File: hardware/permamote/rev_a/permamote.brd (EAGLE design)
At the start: 27 x 60.1 mm, 131 parts, among them J1 TC2030-JLINK-NL, J5 MICRO_USB_B_HIROSE_ZX62R-B-5P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, Q1 PMDXB950UPEL, Q10 PMDXB950UPEL, Q2 PMDXB950UPEL, Q3 PMDXB950UPEL, Q4 PMDXB950UPEL, Q5 PMDXB950UPEL, Q6 PMDXB950UPEL, Q7 PMDXB950UPEL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

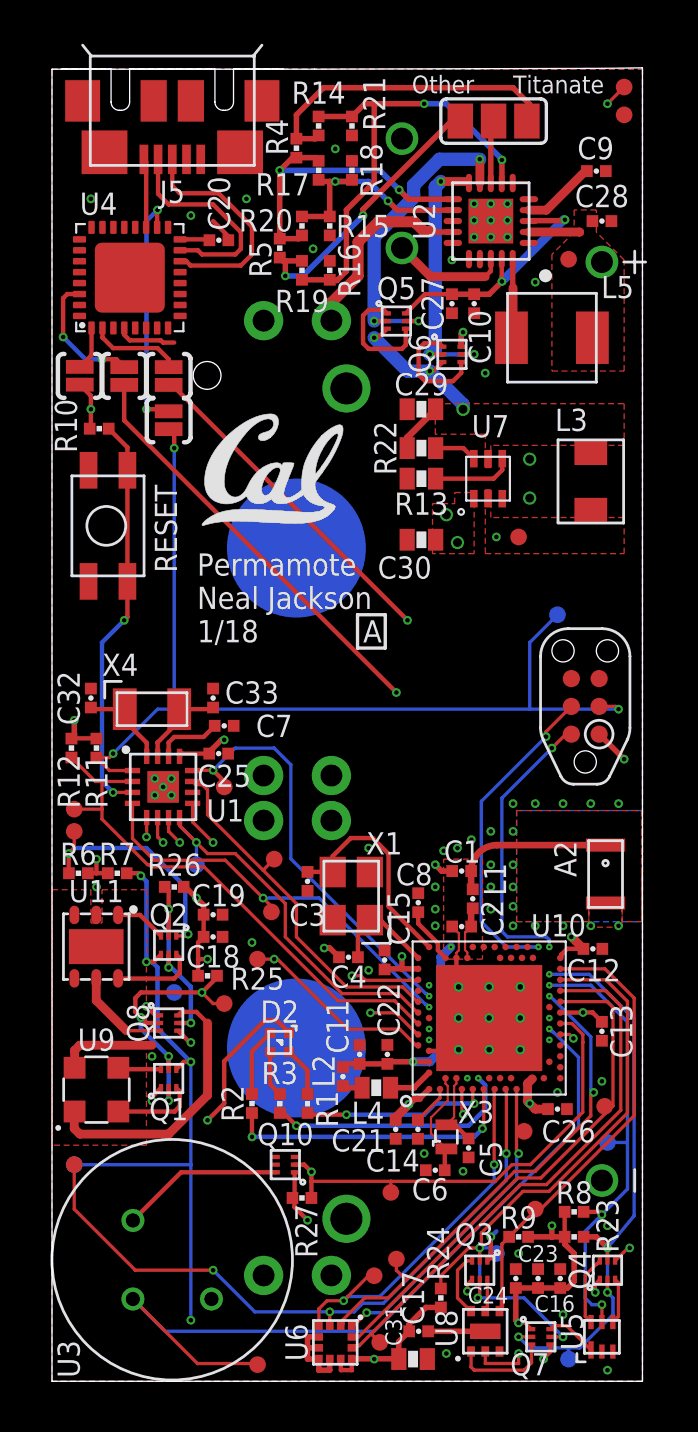
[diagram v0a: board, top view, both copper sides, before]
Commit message: Change attributes to include MPN, fix up BOM
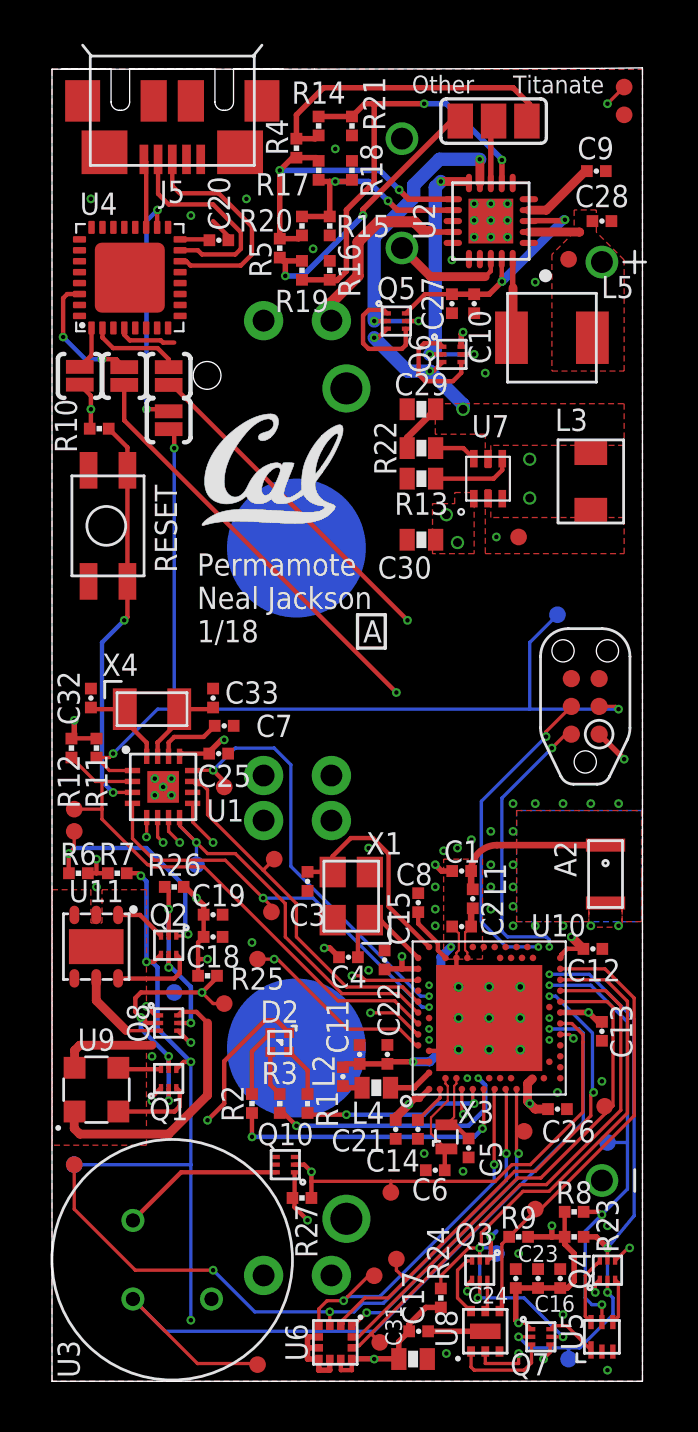
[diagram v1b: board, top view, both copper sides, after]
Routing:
- net PIR_OUT: track 36.9 -> 37.8 mm

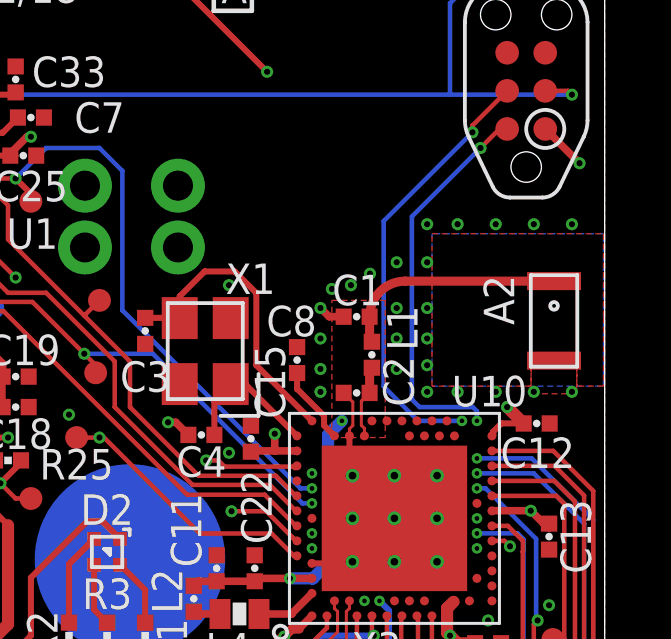
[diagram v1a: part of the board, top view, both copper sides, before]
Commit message: Fix NRF52840 via drill size
Update BOM
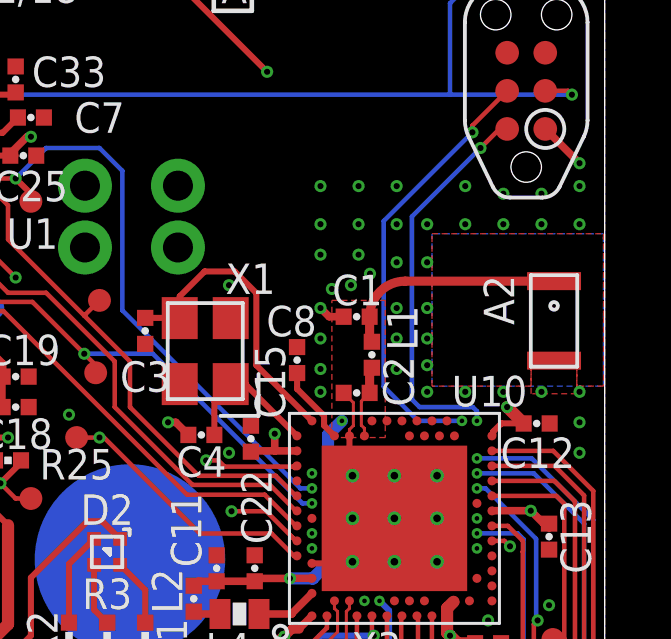
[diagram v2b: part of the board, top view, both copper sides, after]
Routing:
- net GND: track 31.5 -> 31.6 mm, vias 74 -> 88

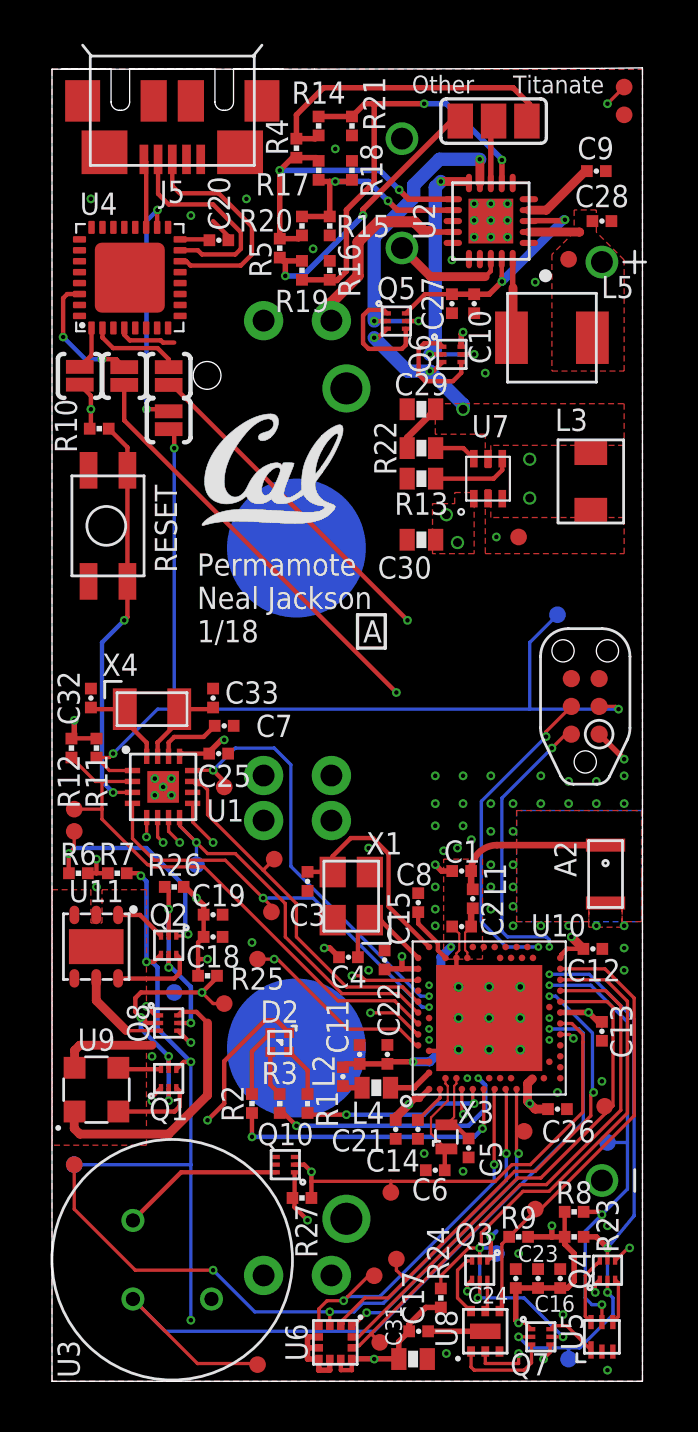
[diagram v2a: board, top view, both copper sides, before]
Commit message: Move silk+testpoints
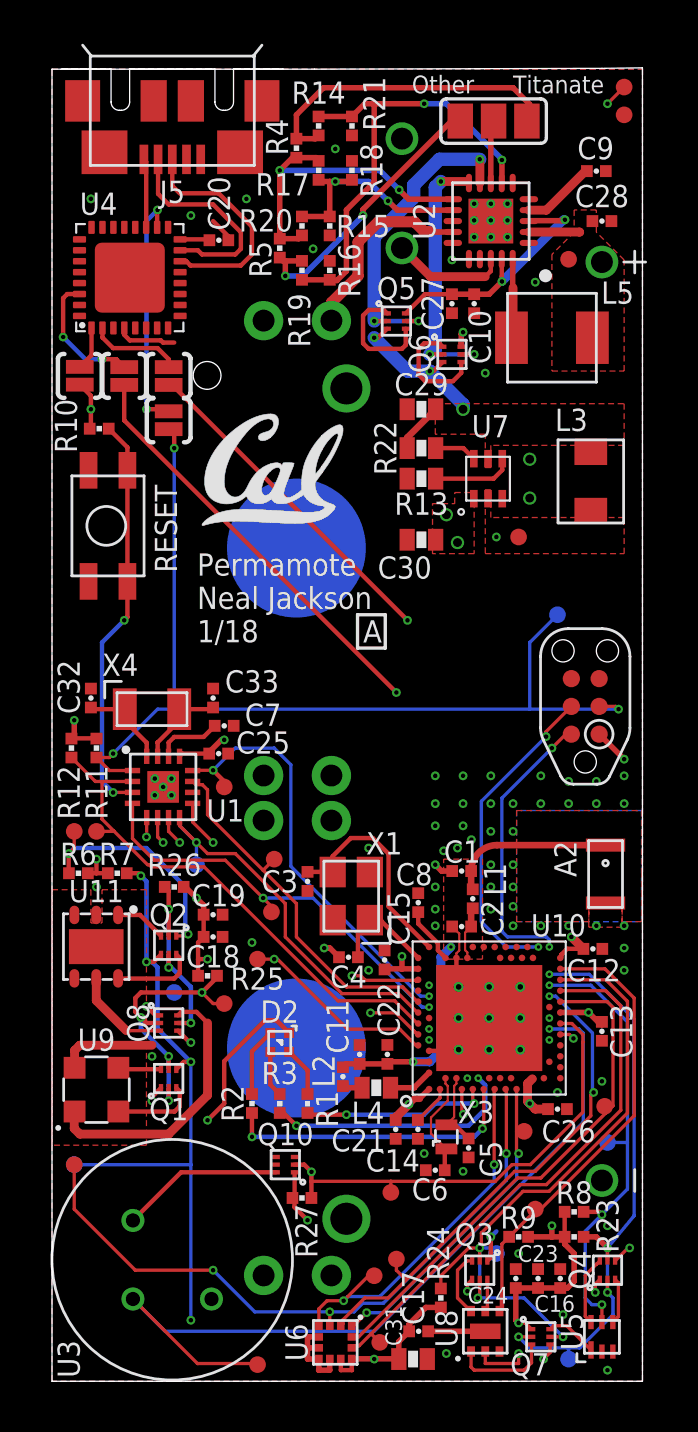
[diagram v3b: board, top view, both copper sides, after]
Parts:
- moved TP16 1.44 mm to (2.03, 25.1)
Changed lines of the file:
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@@
 <?xml version="1.0" encoding="utf-8"?>
 <!DOCTYPE eagle SYSTEM "eagle.dtd">
-<eagle version="8.5.2">
+<eagle version="8.6.0">
 <drawing>
 <settings>
@@
 <attribute name="DIGIKEY" value="490-6197-1-ND" x="11.684" y="22.86" size="1.778" layer="27" rot="R90" display="off"/>
 <attribute name="MPN" value="GRM1555C1H120GA01D " x="11.684" y="22.86" size="1.778" layer="27" rot="R90" display="off"/>
-<attribute name="NAME" x="11.684" y="21.844" size="1.016" layer="25" font="vector" ratio="12" rot="R180" align="bottom-center"/>
+<attribute name="NAME" x="10.414" y="22.352" size="1.016" layer="25" font="vector" ratio="12" align="bottom-center"/>
 </element>
 <element name="C4" library="passives" package="0402_CAP" value="12pF" x="13.557" y="19.392" smashed="yes">
@@
 </element>
 <element name="BT1" library="batteries" package="1020" value="LTOHTC1020" x="16.002" y="54.324" smashed="yes" rot="MR90">
-<attribute name="NAME" x="11.43" y="49.156" size="1.016" layer="22" font="vector" ratio="12" rot="MR0" align="bottom-center"/>
+<attribute name="NAME" x="11.43" y="49.156" size="1.016" layer="26" font="vector" ratio="12" rot="MR0" align="bottom-center"/>
 </element>
 <element name="BT4" library="batteries" package="BH123A" value="BAT_PACKCR123A" x="13.462" y="26.416" smashed="yes" rot="MR90">
@@
 <attribute name="MANUFACTURER" value="MPD" x="13.462" y="26.416" size="1.778" layer="28" rot="MR90" display="off"/>
 <attribute name="MPN" value="BH123A" x="13.462" y="26.416" size="1.778" layer="28" rot="MR90" display="off"/>
-<attribute name="NAME" x="22.606" y="4.826" size="1.016" layer="22" font="vector" ratio="12" rot="MR90"/>
+<attribute name="NAME" x="22.606" y="4.826" size="1.016" layer="26" font="vector" ratio="12" rot="MR90"/>
 </element>
 <element name="U5" library="chips" package="ODFN-6-1.5MMX1.6MM" value="ISL29125" x="25.146" y="2.032" smashed="yes" rot="R90">
@@
 <attribute name="DIGIKEY" value="490-5942-1-ND" x="4.064" y="36.322" size="1.778" layer="27" display="off"/>
 <attribute name="MPN" value="GRM1555C1H470JA01D " x="7.874" y="29.972" size="1.778" layer="27" display="off"/>
-<attribute name="NAME" x="10.16" y="29.464" size="1.016" layer="25" font="vector" ratio="12" align="bottom-center"/>
+<attribute name="NAME" x="9.652" y="29.972" size="1.016" layer="25" font="vector" ratio="12" align="bottom-center"/>
 </element>
 <element name="X4" library="crystals" package="2-SMD" value="ABS07-32.768KHZ-7-T" x="4.572" y="30.734" smashed="yes">
@@
 </element>
 <element name="C32" library="passives" package="0402_CAP" value="DNP" x="1.778" y="31.242" smashed="yes" rot="R90">
-<attribute name="NAME" x="1.27" y="31.242" size="1.016" layer="25" font="vector" ratio="12" rot="R90" align="bottom-center"/>
+<attribute name="NAME" x="1.27" y="31.75" size="1.016" layer="25" font="vector" ratio="12" rot="R90" align="bottom-center"/>
 </element>
 <element name="C33" library="passives" package="0402_CAP" value="DNP" x="7.366" y="31.242" smashed="yes" rot="R90">
-<attribute name="NAME" x="9.144" y="30.988" size="1.016" layer="25" font="vector" ratio="12" align="bottom-center"/>
+<attribute name="NAME" x="9.144" y="31.496" size="1.016" layer="25" font="vector" ratio="12" align="bottom-center"/>
 </element>
 <element name="C25" library="passives" package="0402_CAP" value="1uF" x="7.62" y="28.702" smashed="yes">
 <attribute name="DIGIKEY" value="490-7195-1-ND " x="-2.54" y="27.432" size="1.778" layer="27" display="off"/>
 <attribute name="MPN" value="GRM155R70G105KA12D " x="7.62" y="28.702" size="1.778" layer="27" display="off"/>
-<attribute name="NAME" x="7.874" y="28.194" size="1.016" layer="25" font="vector" ratio="12" rot="R180" align="bottom-center"/>
+<attribute name="NAME" x="9.652" y="29.718" size="1.016" layer="25" font="vector" ratio="12" rot="R180" align="bottom-center"/>
 </element>
 <element name="C17" library="passives" package="0402_CAP" value="0.1uF" x="16.764" y="2.286" smashed="yes">
@@
 <attribute name="DIGIKEY" value="732-3340-1-ND" x="22.86" y="47.72" size="1.778" layer="27" rot="R180" display="off"/>
 <attribute name="MPN" value="74437324220 " x="22.86" y="47.72" size="1.778" layer="27" rot="R180" display="off"/>
-<attribute name="NAME" x="25.114" y="49.53" size="1.016" layer="25" font="vector" ratio="12"/>
+<attribute name="NAME" x="25.114" y="49.276" size="1.016" layer="25" font="vector" ratio="12"/>
 <attribute name="VALUE" x="26.035" y="52.8" size="1.27" layer="27" rot="R180"/>
 </element>
@@
 <attribute name="DIGIKEY" value="311-10KJRCT-ND " x="2.032" y="28.956" size="1.778" layer="27" rot="R90" display="off"/>
 <attribute name="MPN" value="RC0402JR-0710KL" x="2.032" y="28.956" size="1.778" layer="27" rot="R90" display="off"/>
-<attribute name="NAME" x="2.54" y="27.432" size="1.016" layer="25" font="vector" ratio="12" rot="R90" align="bottom-center"/>
+<attribute name="NAME" x="2.54" y="26.924" size="1.016" layer="25" font="vector" ratio="12" rot="R90" align="bottom-center"/>
 <attribute name="VALUE" x="3.429" y="28.956" size="1.016" layer="27" font="vector" ratio="12" rot="R90" align="bottom-center"/>
 </element>
@@
 <attribute name="MOUSER" value="712-BAT-HLD-001-THM" x="11.176" y="15.24" size="1.778" layer="28" rot="MR270" display="off"/>
 <attribute name="MPN" value="BAT-HLD-001-THM" x="11.176" y="15.24" size="1.778" layer="28" rot="MR270" display="off"/>
-<attribute name="NAME" x="21.844" y="15.24" size="1.016" layer="26" font="vector" ratio="12" rot="MR90" align="bottom-center"/>
+<attribute name="NAME" x="17.018" y="24.384" size="1.016" layer="26" font="vector" ratio="12" rot="MR0" align="bottom-center"/>
 </element>
 <element name="BT3" library="batteries" package="BAT-HLD-002-THM" value="BAT-HLD-002-THM" x="11.176" y="38.1" smashed="yes" rot="MR270">
@@
 <attribute name="MOUSER" value="712-BAT-HLD-001-THM" x="11.176" y="38.1" size="1.778" layer="28" rot="MR270" display="off"/>
 <attribute name="MPN" value="BAT-HLD-001-THM" x="11.176" y="38.1" size="1.778" layer="28" rot="MR270" display="off"/>
-<attribute name="NAME" x="21.803" y="38.1" size="1.016" layer="26" font="vector" ratio="12" rot="MR90" align="bottom-center"/>
+<attribute name="NAME" x="17.018" y="27.94" size="1.016" layer="26" font="vector" ratio="12" rot="MR0" align="bottom-center"/>
 </element>
 <element name="R19" library="passives" package="0402_RES" value="DNP" x="11.43" y="50.8" smashed="yes" rot="R90">
 <attribute name="DIGIKEY" value="YAG3306CT-ND" x="11.43" y="50.8" size="1.778" layer="27" font="vector" ratio="12" rot="R90" display="off"/>
-<attribute name="NAME" x="11.43" y="49.911" size="1.016" layer="25" font="vector" ratio="12" rot="R180" align="bottom-center"/>
+<attribute name="NAME" x="10.795" y="48.514" size="1.016" layer="25" font="vector" ratio="12" rot="R270" align="bottom-center"/>
 <attribute name="VALUE" x="12.827" y="50.8" size="1.016" layer="27" font="vector" ratio="12" rot="R90" align="bottom-center"/>
 </element>
@@
 <attribute name="DIGIKEY" value="311-10KJRCT-ND " x="0.889" y="28.956" size="1.778" layer="27" rot="R90" display="off"/>
 <attribute name="MPN" value="RC0402JR-0710KL" x="0.889" y="28.956" size="1.778" layer="27" rot="R90" display="off"/>
-<attribute name="NAME" x="1.27" y="27.432" size="1.016" layer="25" font="vector" ratio="12" rot="R90" align="bottom-center"/>
+<attribute name="NAME" x="1.27" y="26.924" size="1.016" layer="25" font="vector" ratio="12" rot="R90" align="bottom-center"/>
 <attribute name="VALUE" x="2.286" y="28.956" size="1.016" layer="27" font="vector" ratio="12" rot="R90" align="bottom-center"/>
 </element>
@@
 <element name="TP14" library="headers" package="PAD.03X.03" value="TEST-POINT" x="10.033" y="21.463"/>
 <element name="TP15" library="headers" package="PAD.03X.03" value="TEST-POINT" x="6.604" y="23.622" rot="MR0"/>
-<element name="TP16" library="headers" package="PAD.03X.03" value="TEST-POINT" x="1.016" y="26.162"/>
+<element name="TP16" library="headers" package="PAD.03X.03" value="TEST-POINT" x="2.032" y="25.146"/>
 <element name="TP17" library="headers" package="PAD.03X.03" value="TEST-POINT" x="23.114" y="35.052" rot="MR0"/>
 <element name="TP18" library="headers" package="PAD.03X.03" value="TEST-POINT" x="25.273" y="12.573"/>
@@
 <wire x1="2.286" y1="27.428" x2="1.98393125" y2="27.428" width="0.1524" layer="1"/>
 <wire x1="1.98393125" y1="27.428" x2="0.889" y2="28.52293125" width="0.1524" layer="1"/>
-<wire x1="2.286" y1="27.428" x2="2.286" y2="26.162" width="0.1524" layer="1"/>
-<wire x1="2.286" y1="26.162" x2="2.286" y2="25.705225" width="0.1524" layer="1"/>
-<wire x1="2.286" y1="25.705225" x2="4.369225" y2="23.622" width="0.1524" layer="1"/>
+<wire x1="2.286" y1="27.428" x2="2.286" y2="25.705225" width="0.1524" layer="1"/>
+<wire x1="2.286" y1="25.705225" x2="2.8196125" y2="25.1716125" width="0.1524" layer="1"/>
 <contactref element="U10" pad="A12"/>
+<wire x1="2.8196125" y1="25.1716125" x2="4.369225" y2="23.622" width="0.1524" layer="1"/>
 <wire x1="4.369225" y1="23.622" x2="4.44574375" y2="23.622" width="0.1524" layer="1"/>
 <wire x1="4.54734375" y1="23.5204" x2="4.44574375" y2="23.622" width="0.1524" layer="1"/>
@@
 <wire x1="16.70658125" y1="16.36" x2="15.66758125" y2="17.399" width="0.1524" layer="1"/>
 <contactref element="TP16" pad="P$1"/>
-<wire x1="1.016" y1="26.162" x2="2.286" y2="26.162" width="0.1524" layer="1"/>
+<wire x1="2.032" y1="25.146" x2="2.794" y2="25.146" width="0.1524" layer="1"/>
+<wire x1="2.794" y1="25.146" x2="2.8196125" y2="25.1716125" width="0.1524" layer="1"/>
 </signal>
 <signal name="SDA">

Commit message: Smaller silk + fixed outline
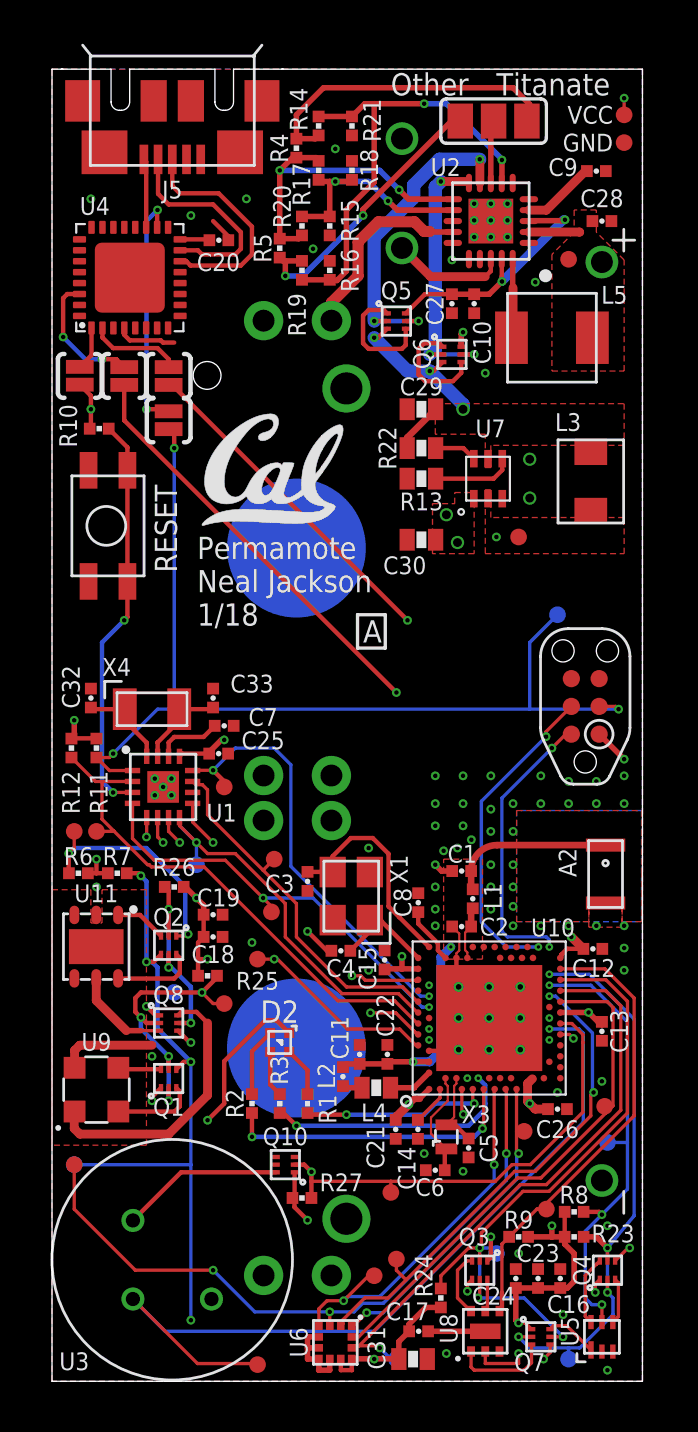
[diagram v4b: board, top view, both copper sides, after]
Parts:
- moved TP26 1.27 mm to (26.2, 57.9)
- moved TP27 1.27 mm to (26.2, 56.6)
- moved TP19 1.08 mm to (15.7, 1.02), flipped to the bottom
- moved TP21 0.51 mm to (22.6, 7.87)
- moved C4 0.46 mm to (13.2, 19.7)
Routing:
- net ACC_INT2: track 25.2 -> 26.6 mm, vias 0 -> 1
- net GND: track 31.6 -> 32.2 mm
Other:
- board size 27 x 60.1 mm -> 27 x 60 mm
- board text added: "GND"
- board text added: "VCC"
